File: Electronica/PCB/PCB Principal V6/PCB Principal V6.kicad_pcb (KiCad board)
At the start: 2 copper layers, 140 x 78.7 mm, 22 parts, among them J1 Conexion Sensores, J10 Conn_01x01, J2 Power Monster, J3 On/Off General, J4 Power Input 2, J5 IDC Placa Botones, J6 Power Input 1, J7 Conn_01x01, J8 Conn_01x01, J9 Conn_01x01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

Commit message: ?
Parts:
- moved J6 2.33 mm to (88.5, 92.2)
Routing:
- net MOTORES: track 184.7 -> 199.6 mm
- net +5V: track 219.6 -> 230.4 mm
- net VNano: track 177.3 -> 185.4 mm
- net Net-(D4-A): track 7.04 -> 9.81 mm
- net Net-(J2-Pin_2): track 14.6 -> 17.2 mm
- net PI+: track 27.7 -> 25.4 mm
- net Net-(J4-Pin_2): track 9.82 -> 12.1 mm
- net LED4: track 27.4 -> 29.6 mm
- net LED3: track 21.0 -> 22.7 mm
- net GND: track 440.6 -> 439.5 mm
- net LED2: track 14.5 -> 15.2 mm
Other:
- board size 140 x 78.7 mm -> 141.2 x 78.7 mm

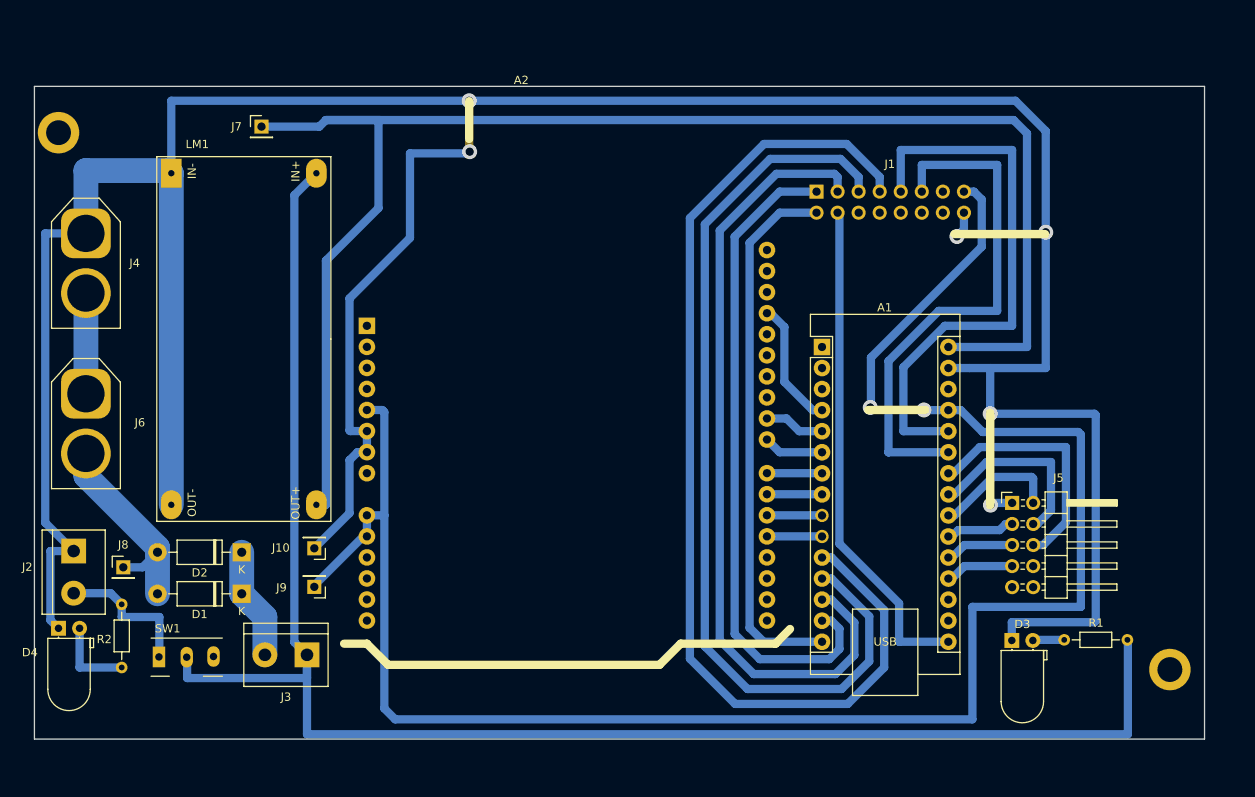
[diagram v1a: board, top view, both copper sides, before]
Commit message: Placa sensores y placa principar terminada
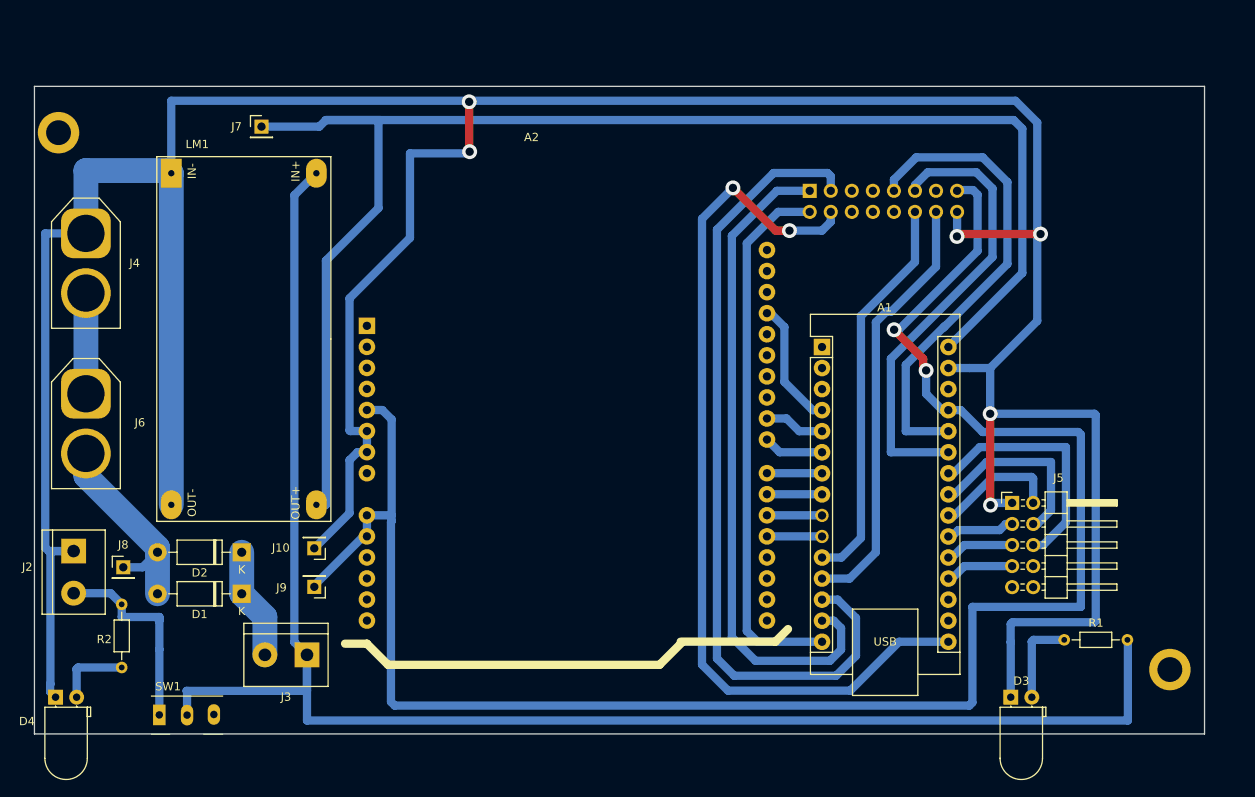
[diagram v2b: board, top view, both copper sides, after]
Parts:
- moved D4 8.32 mm to (84.8, 128.8)
- moved SW1 6.99 mm to (98.7, 131.0)
- moved D3 6.85 mm to (200.1, 128.8)
- moved J1 0.83 mm to (175.8, 67.7)
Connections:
- A1 pad 12: ECHO 2 -> TRIG 1
- A1 pad 13: TRIG 1 -> ECHO 2
- J1 pad 12: ECHO 5 -> ECHO 1
- J1 pad 14: TRIG 5 -> TRIG 1
- J1 pad 3: TRIG 1 -> ECHO 2
- J1 pad 5: ECHO 2 -> TRIG 5
- J1 pad 7: ECHO 1 -> ECHO 5
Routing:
- net ECHO 1: track 127.7 -> 47.7 mm
- net TRIG 3: track 60.8 -> 108.1 mm, vias 0 -> 2
- net TRIG 1: track 96.3 -> 52.2 mm
- net ECHO 2: track 111.8 -> 98.4 mm
- net GND: track 439.5 -> 450.5 mm
- net CNY 1: track 68.0 -> 58.0 mm
- net +5V: track 230.4 -> 221.5 mm
- net CNY 2: track 63.8 -> 55.3 mm
- net Net-(J2-Pin_2): track 17.2 -> 24.7 mm
- net Net-(D3-A): track 3.82 -> 10.7 mm
- net VNano: track 185.4 -> 179.4 mm
- net MOTORES: track 199.6 -> 198.4 mm
- net Net-(D4-A): track 9.81 -> 8.94 mm
- net TRIG 2: track 79.4 -> 80.2 mm
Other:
- board size 141.2 x 78.7 mm -> 141.2 x 78.1 mm

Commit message: PCB V6 ACTUALIZADA
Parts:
- added U1: 74HC595, 74HC595N_DIP16_:DIP16-2.54-20.32X5.84MM, B.Cu at (190.6, 73.6)
- moved J1 12.1 mm to (181.7, 57.1)
- moved R1 11.9 mm to (202.5, 124.2), turned to 0 degrees
- moved J5 9.45 mm to (207.1, 98.8)
- moved A1 5.91 mm to (183.2, 86.1)
- moved ? 5.82 mm to (225.1, 125.1)
- moved D3 5.82 mm to (205.9, 128.4)
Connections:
- A1 pad 12: TRIG 1 -> ECHO 2
- A1 pad 13: ECHO 2 -> ECHO 3
- A1 pad 14: TRIG 2 -> Data
- A1 pad 15: ECHO 3 -> Latch
- A1 pad 16: TRIG 3 -> Clock
- A1 pad 19: LED1 -> unconnected-(A1-A0-Pad19)
- A1 pad 20: BTN1 -> ECHO 4
- A1 pad 21: BTN2 -> ECHO 5
- A1 pad 22: LED2 -> LED4
- A1 pad 23: LED3 -> BTN1
- A1 pad 24: LED4 -> BTN2
- A1 pad 25: CNY 2 -> CNY 1
- A1 pad 26: CNY 1 -> CNY 2
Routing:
- net TRIG 3: track 108.1 -> 10.2 mm, vias 2 -> 0
- net LED1: track 8.32 -> 89.4 mm, vias 0 -> 4
- net TRIG 2: track 80.2 -> 17.4 mm
- net Latch: track 0.00 -> 52.9 mm
- net Data: track 0.00 -> 49.3 mm
- net Clock: track 0.00 -> 46.2 mm
- net TRIG 1: track 52.2 -> 10.2 mm
- net ECHO 3: track 65.5 -> 103.0 mm, vias 0 -> 2
- net VNano: track 179.4 -> 216.1 mm, vias 0 -> 4
- net LED2: track 15.2 -> 48.9 mm, vias 0 -> 2
- net MOTORES: track 198.4 -> 170.2 mm
- net ECHO 1: track 47.7 -> 75.1 mm, vias 0 -> 4
- net LED3: track 22.7 -> 0.00 mm
- net CNY 1: track 58.0 -> 68.4 mm
- net TRIG 4: track 0.00 -> 10.2 mm
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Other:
- board outline removed
